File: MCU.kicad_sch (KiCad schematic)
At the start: 15 parts, among them M1 Conn_01x04, M2 Conn_01x04, M3 Conn_01x04, U2 ESP32-S3-DevKitC

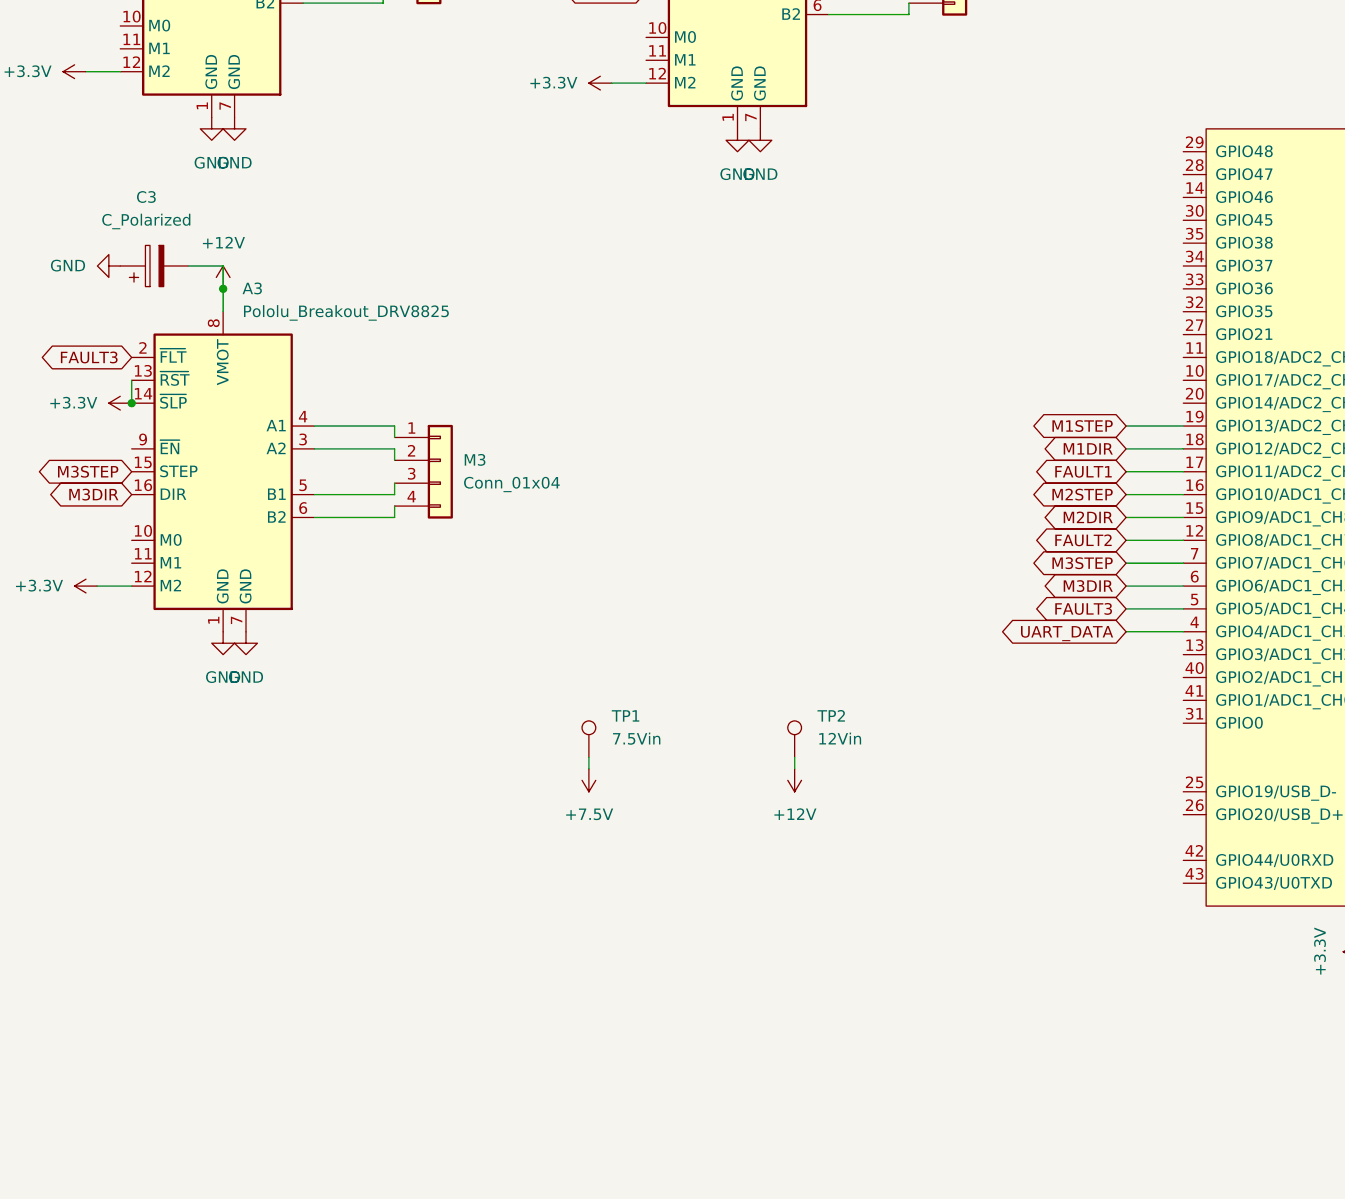
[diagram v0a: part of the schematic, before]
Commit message: Changed routings and added encoder ports (pwm output pins).
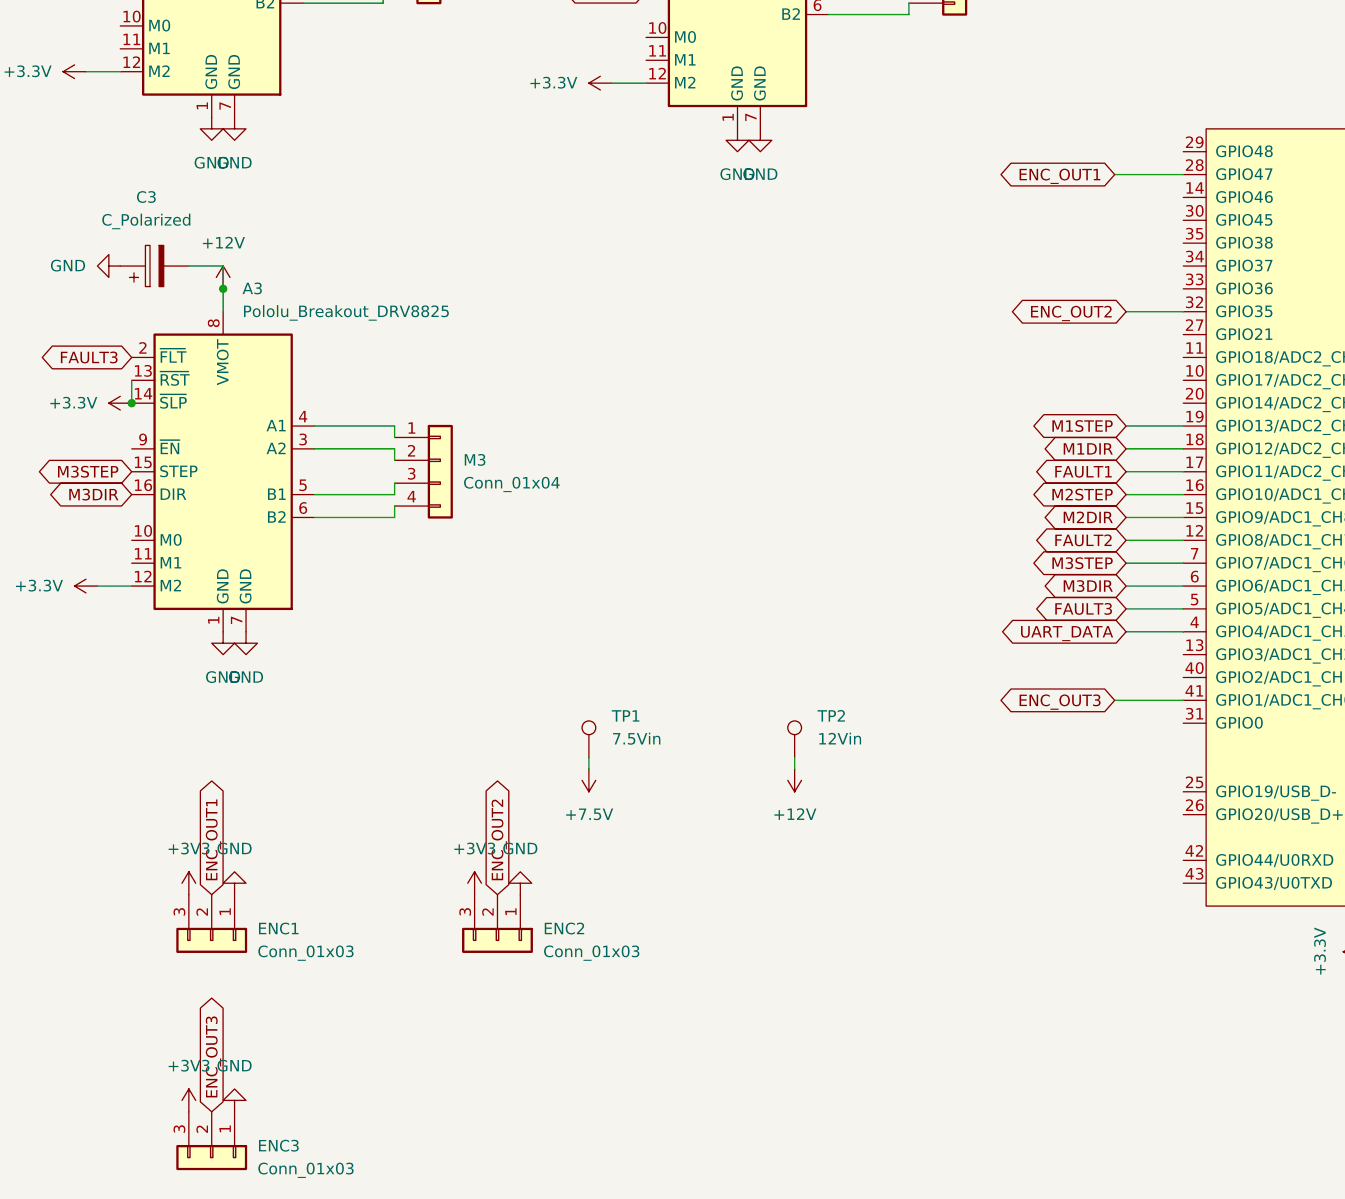
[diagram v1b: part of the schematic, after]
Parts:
- added ENC1, ENC2, ENC3: Conn_01x03, Connector_PinHeader_2.54mm:PinHeader_1x03_P2.54mm_Vertical, symbol Connector_Generic:Conn_01x03
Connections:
- net GND: now also ENC1.1 (Pin_1), ENC2.1 (Pin_1), ENC3.1 (Pin_1)
- net ENC_OUT1: now reaches U2.28 (GPIO47)
- net ENC_OUT1: now also ENC1.2 (Pin_2)
- net ENC_OUT2: now reaches U2.32 (GPIO35)
- net ENC_OUT2: now also ENC2.2 (Pin_2)
- net ENC_OUT3: now reaches U2.41 (GPIO1/ADC1_CH0)
- net ENC_OUT3: now also ENC3.2 (Pin_2)
- new net +3V3: ENC1.3 (Pin_3), ENC2.3 (Pin_3), ENC3.3 (Pin_3)

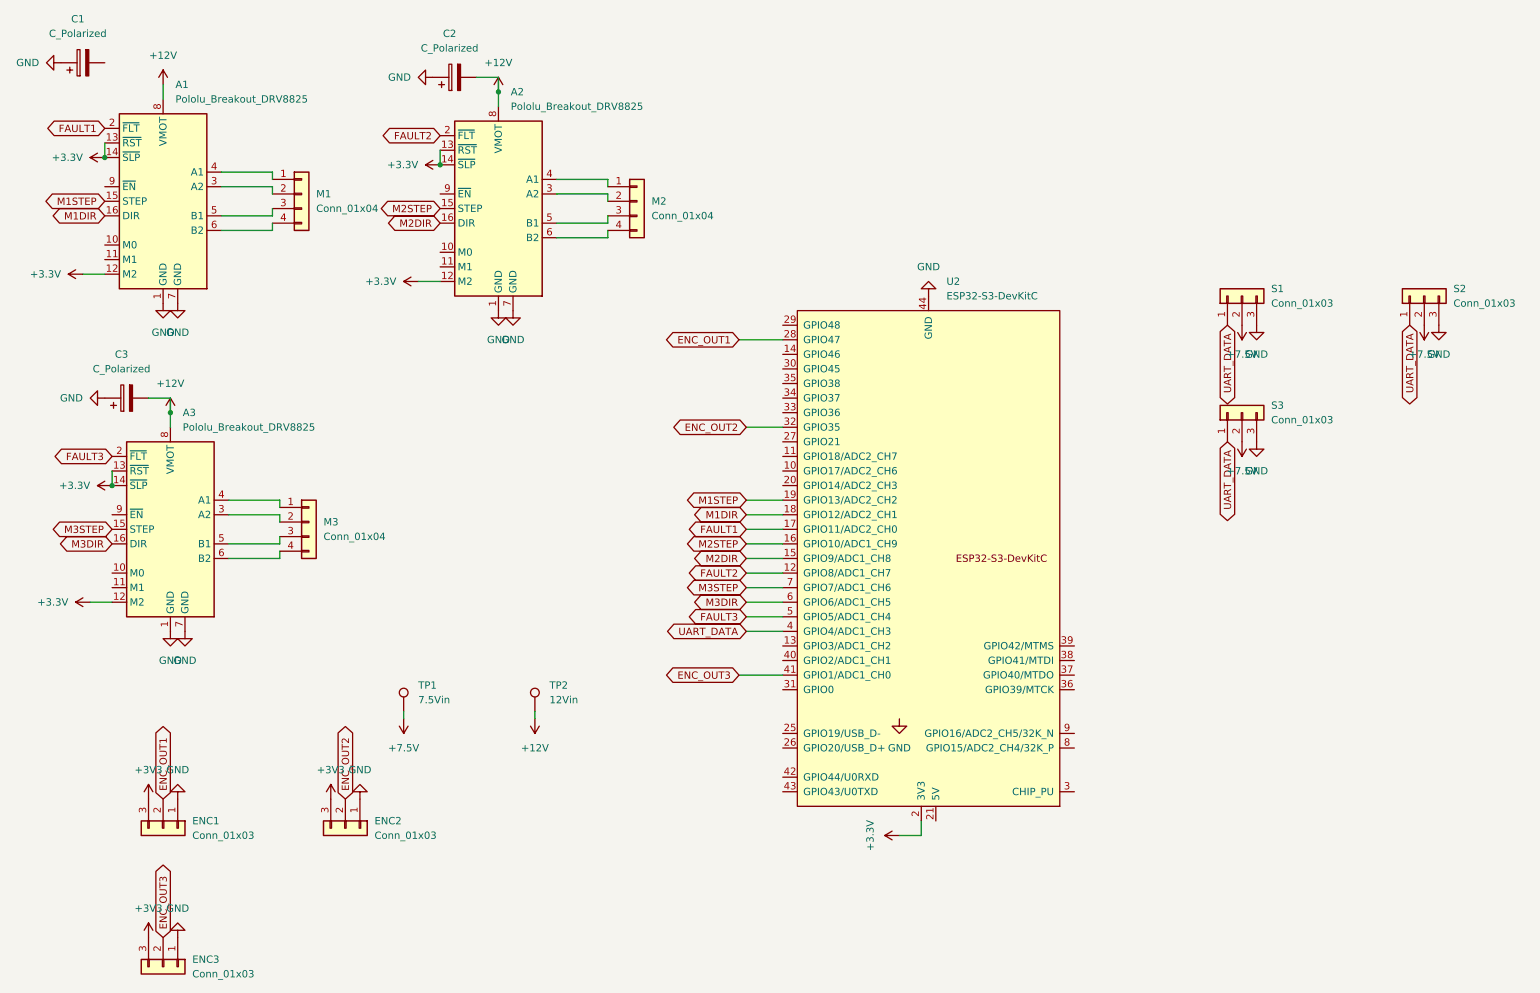
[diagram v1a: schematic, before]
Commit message: fixed trace widths
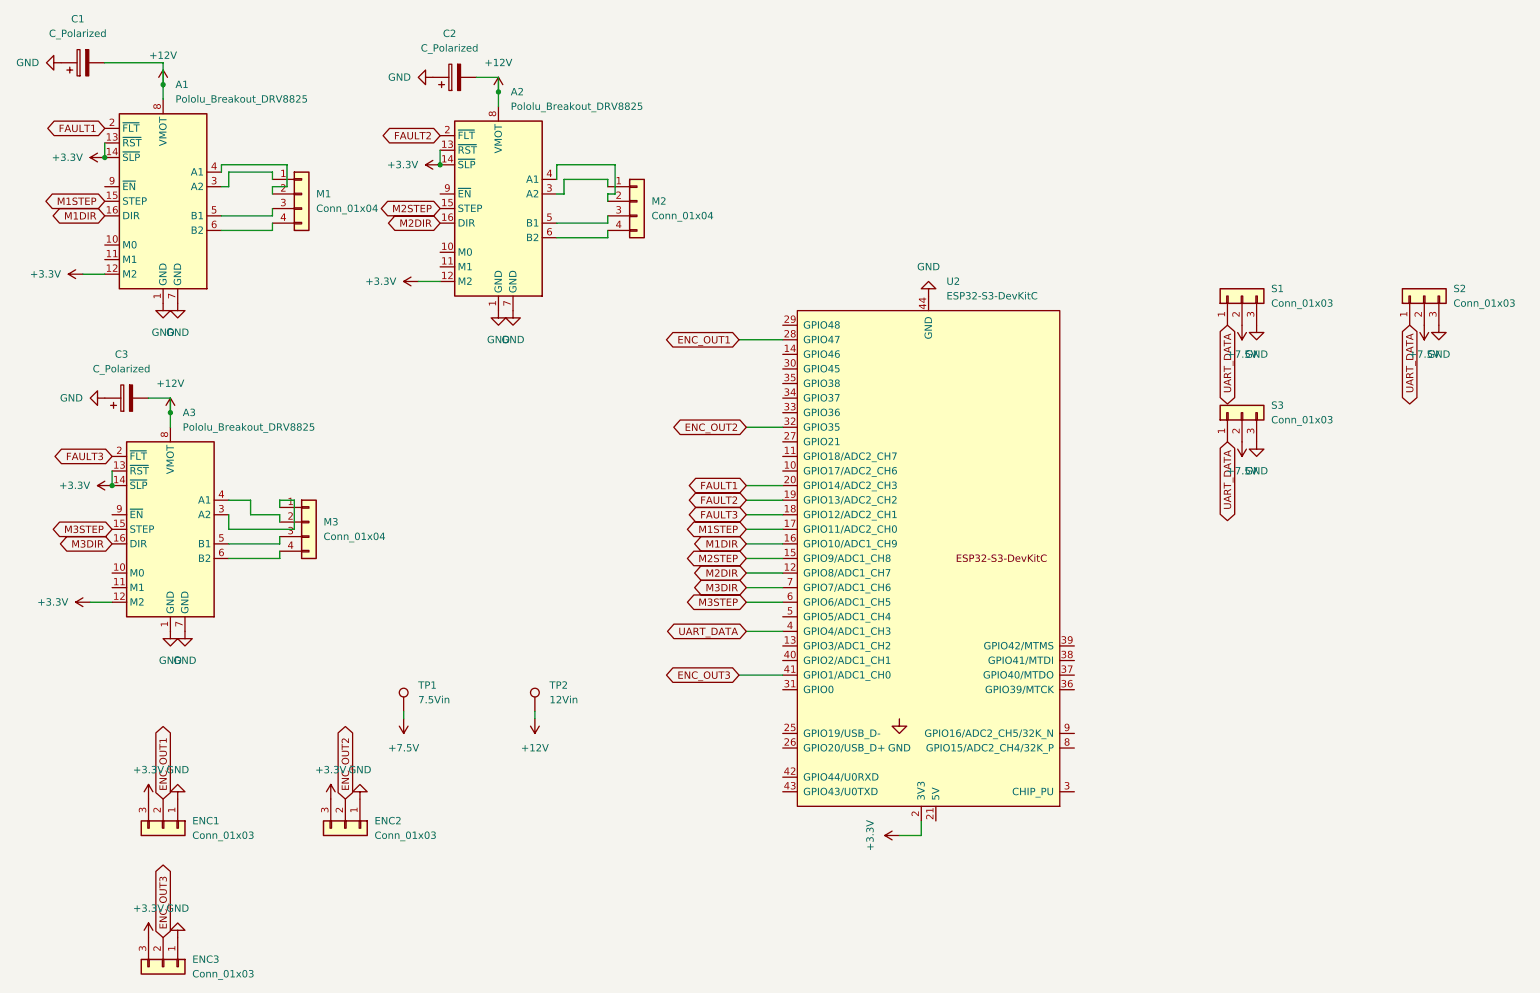
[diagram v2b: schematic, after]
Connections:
- net +3V3 is gone; now on net +3.3V: ENC1.3 (Pin_3), ENC2.3 (Pin_3), ENC3.3 (Pin_3)
- net +12V: now also C1.2
- net FAULT1: now also U2.20 (GPIO14/ADC2_CH3); no longer U2.17 (GPIO11/ADC2_CH0)
- net FAULT2: now also U2.19 (GPIO13/ADC2_CH2); no longer U2.12 (GPIO8/ADC1_CH7)
- net FAULT3: now also U2.18 (GPIO12/ADC2_CH1); no longer U2.5 (GPIO5/ADC1_CH4)
- net M1DIR: now also U2.16 (GPIO10/ADC1_CH9); no longer U2.18 (GPIO12/ADC2_CH1)
- net M1STEP: now also U2.17 (GPIO11/ADC2_CH0); no longer U2.19 (GPIO13/ADC2_CH2)
- net M2DIR: now also U2.12 (GPIO8/ADC1_CH7); no longer U2.15 (GPIO9/ADC1_CH8)
- net M2STEP: now also U2.15 (GPIO9/ADC1_CH8); no longer U2.16 (GPIO10/ADC1_CH9)
- net M3DIR: now also U2.7 (GPIO7/ADC1_CH6); no longer U2.6 (GPIO6/ADC1_CH5)
- net M3STEP: now also U2.6 (GPIO6/ADC1_CH5); no longer U2.7 (GPIO7/ADC1_CH6)
- net at M3.1 (Pin_1): now also A3.3 (A2); no longer A3.4 (A1)
- net at M3.2 (Pin_2): now also A3.4 (A1); no longer A3.3 (A2)
- net at M2.1 (Pin_1): now also A2.3 (A2); no longer A2.4 (A1)
- net at M2.2 (Pin_2): now also A2.4 (A1); no longer A2.3 (A2)
- net at A1.3 (A2): now also M1.1 (Pin_1); no longer M1.2 (Pin_2)
- net at A1.4 (A1): now also M1.2 (Pin_2); no longer M1.1 (Pin_1)
